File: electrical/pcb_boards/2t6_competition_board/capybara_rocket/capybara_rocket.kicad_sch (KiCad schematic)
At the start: 1 part, among them U1 WRL-11812

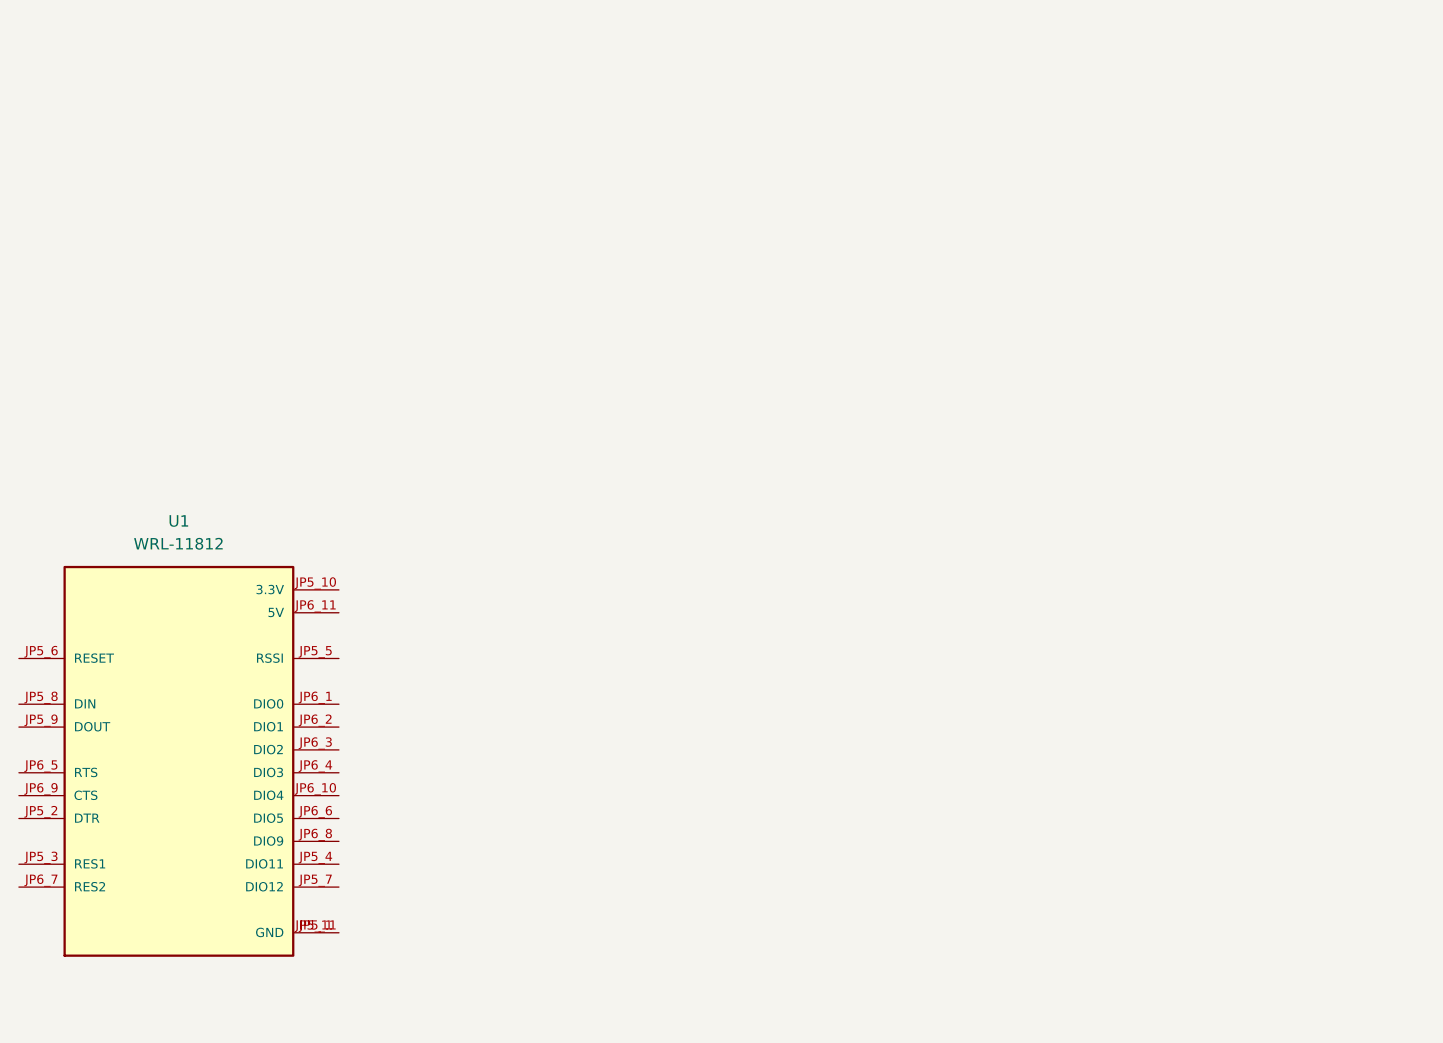
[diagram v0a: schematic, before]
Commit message: Adding new KiCad symbols and footprints and initial PCB dimension work
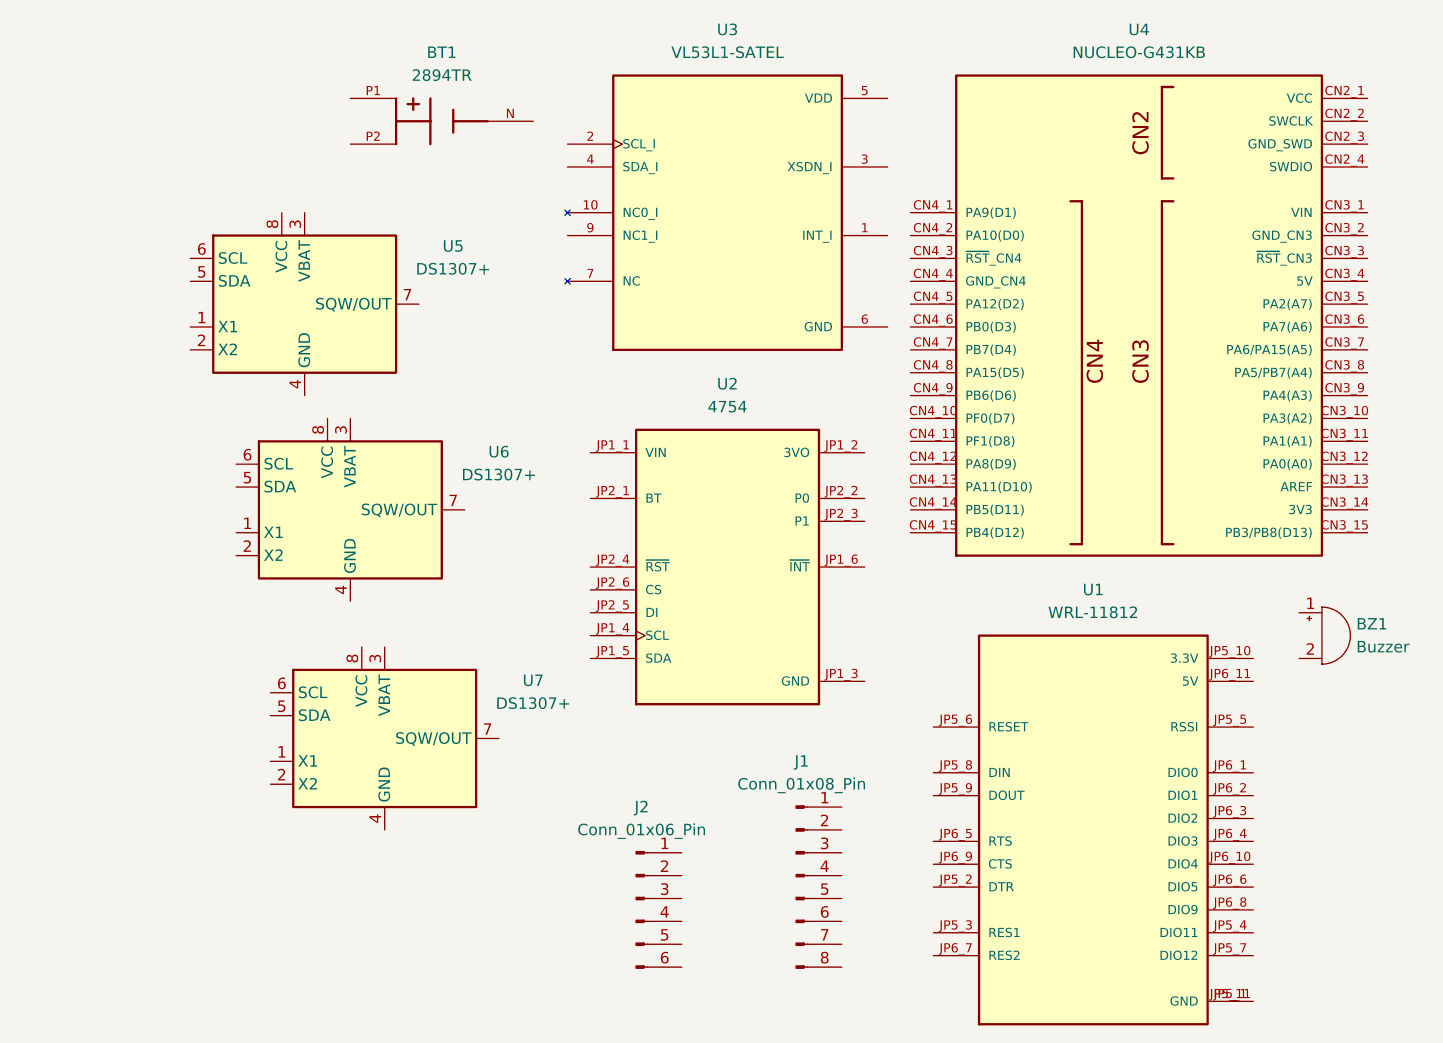
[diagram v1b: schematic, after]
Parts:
- added BT1: 2894TR, RSX_CanSat_Custom_KiCad_Footprints:BAT_2894TR, symbol RSX_CanSat_Custom_KiCad_Symbols:2894TR
- added BZ1: Buzzer, Buzzer_Beeper:Buzzer_TDK_PS1240P02BT_D12.2mm_H6.5mm, symbol Device:Buzzer
- added J1: Conn_01x08_Pin, RSX_CanSat_Custom_KiCad_Footprints:Adafruit_BMP581, symbol Connector:Conn_01x08_Pin
- added J2: Conn_01x06_Pin, RSX_CanSat_Custom_KiCad_Footprints:MODULE_904, symbol Connector:Conn_01x06_Pin
- added U2: 4754, RSX_CanSat_Custom_KiCad_Footprints:MODULE_4754, symbol RSX_CanSat_Custom_KiCad_Symbols:4754
- added U3: VL53L1-SATEL, RSX_CanSat_Custom_KiCad_Footprints:MODULE_VL53L1X-SATEL, symbol RSX_CanSat_Custom_KiCad_Symbols:VL53L1-SATEL
- added U4: NUCLEO-G431KB, RSX_CanSat_Custom_KiCad_Footprints:MODULE_NUCLEO-G431KB, symbol RSX_CanSat_Custom_KiCad_Symbols:NUCLEO-G431KB
- added U5, U6, U7: DS1307+, Package_DIP:DIP-8_W7.62mm, symbol Timer_RTC:DS1307+
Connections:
- new net: U3.7 (NC), U3.8 (NC)
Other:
- moved on the sheet: U1

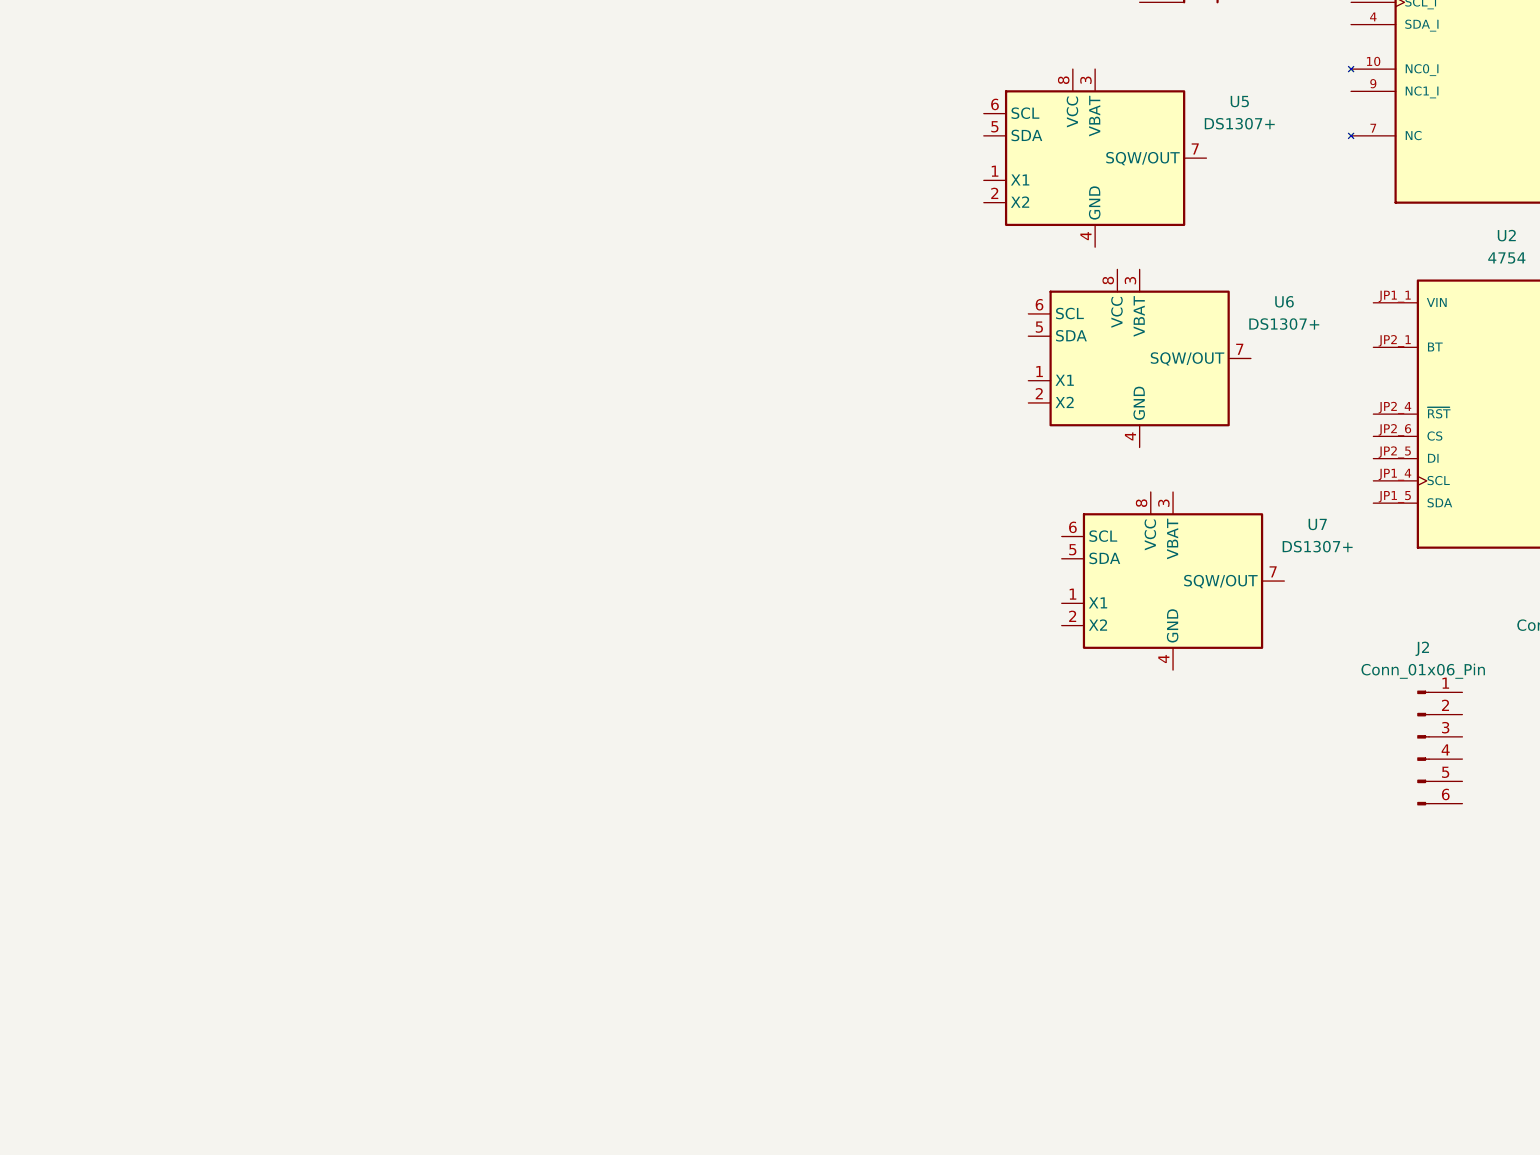
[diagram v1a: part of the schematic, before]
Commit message: pcb board update w/ new symbols, footprints, and 3dmodels
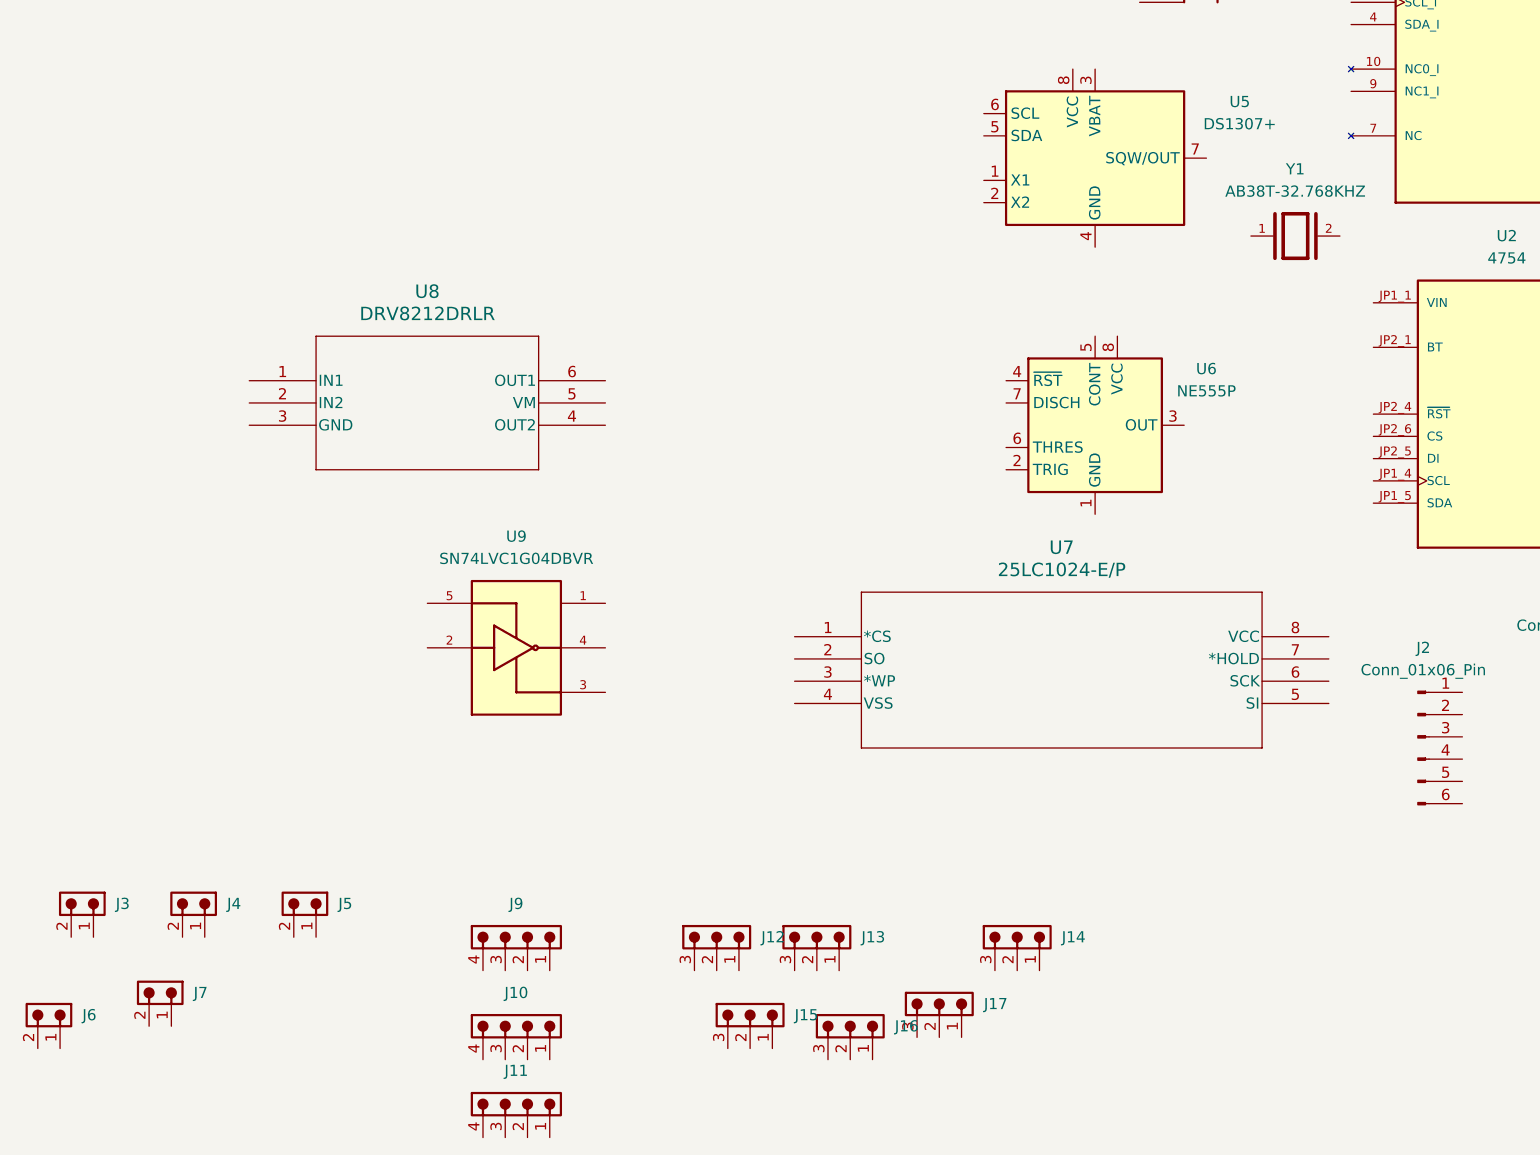
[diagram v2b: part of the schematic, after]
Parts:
- removed U6, U7: DS1307+, Package_DIP:DIP-8_W7.62mm, symbol Timer_RTC:DS1307+
- added J10, J11, J9: Wurth_M4_62000411622, RSX_CanSat_Custom_KiCad_Footprints:J_Wurth_WR-WTB_62000411622, symbol RSX_CanSat_Custom_KiCad_Symbols:Wurth_M4_62000411622
- added J12, J13, J14, J15, J16, J17: Wurth_M3_62000311622, RSX_CanSat_Custom_KiCad_Footprints:J_Wurth_WR-WTB_62000311622, symbol RSX_CanSat_Custom_KiCad_Symbols:Wurth_M3_62000311622
- added J3, J4, J5, J6, J7: Wurth_M2_62000211622, RSX_CanSat_Custom_KiCad_Footprints:J_Wurth_WR-WTB_62000211622, symbol RSX_CanSat_Custom_KiCad_Symbols:Wurth_M2_62000211622
- added U6: NE555P, Package_DIP:DIP-8_W7.62mm, symbol Timer:NE555P
- added U7: 25LC1024-E/P, RSX_CanSat_Custom_KiCad_Footprints:PDIP8_300MC_MCH, symbol RSX_CanSat_Custom_KiCad_Symbols:25LC1024-E_P
- added U8: DRV8212DRLR, RSX_CanSat_Custom_KiCad_Footprints:SOT6_DRV8212_TEX, symbol RSX_CanSat_Custom_KiCad_Symbols:DRV8212DRLR
- added U9: SN74LVC1G04DBVR, RSX_CanSat_Custom_KiCad_Footprints:SOT95P280X145-5N, symbol RSX_CanSat_Custom_KiCad_Symbols:SN74LVC1G04DBVR
- added Y1: AB38T-32.768KHZ, RSX_CanSat_Custom_KiCad_Footprints:XTAL_AB38T-32.768KHZ, symbol RSX_CanSat_Custom_KiCad_Symbols:AB38T-32.768KHZ
- BZ1: footprint Buzzer_Beeper:Buzzer_TDK_PS1240P02BT_D12.2mm_H6.5mm -> Buzzer_Beeper:Buzzer_12x9.5RM7.6
- U1: footprint RSX_CanSat_Custom_KiCad_Footprints:MODULE_WRL-11812 -> RSX_CanSat_Custom_KiCad_Footprints:SparkFun_XBee_Explorer_Regulated
- U2: footprint RSX_CanSat_Custom_KiCad_Footprints:MODULE_4754 -> RSX_CanSat_Custom_KiCad_Footprints:Adafruit_BNO085
- U3: footprint RSX_CanSat_Custom_KiCad_Footprints:MODULE_VL53L1X-SATEL -> RSX_CanSat_Custom_KiCad_Footprints:J_Wurth_WR-WTB_62000411622
